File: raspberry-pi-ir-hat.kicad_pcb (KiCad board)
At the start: 2 copper layers, 56.1 x 52.3 mm, 16 parts, among them J1 IO, J2 TX, J3 RX, J4 RX_JMP, J5 TX_JMP, J6 RW_JMP, J7 Raspberry_Pi_2_3

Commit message: fix drc
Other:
- outline, holes or cut-outs redrawn
- rule pad_to_mask_clearance: 0.05 -> 0.0762
- board text added: "Add jumper for write"
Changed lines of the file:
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@@
   (general
     (thickness 1.6)
-    (drawings 10)
+    (drawings 15)
     (tracks 87)
     (zones 0)
@@
     (pad_size 1.524 1.524)
     (pad_drill 0.762)
-    (pad_to_mask_clearance 0.05)
+    (pad_to_mask_clearance 0.0762)
+    (solder_mask_min_width 0.1016)
     (aux_axis_origin 0 0)
     (visible_elements FFFFFF7F)
@@
     (descr "Through hole straight socket strip, 1x02, 2.54mm pitch, single row (from Kicad 4.0.7), script generated")
     (tags "Through hole socket strip THT 1x02 2.54mm single row")
-    (fp_text reference J6 (at 0 -2.77) (layer F.SilkS)
+    (fp_text reference J6 (at 2.54 1.27 90) (layer F.SilkS)
       (effects (font (size 1 1) (thickness 0.15)))
     )
@@
       (effects (font (size 1 1) (thickness 0.15)))
     )
+    (fp_line (start -3.2766 6.5) (end -3.2766 -6.5) (layer F.CrtYd) (width 0.12))
     (fp_line (start -3.3 -6) (end 7 -6) (layer F.SilkS) (width 0.12))
     (fp_line (start 7 -6) (end 7 6) (layer F.SilkS) (width 0.12))
@@
     (fp_line (start -3.2766 -6.5) (end 7.5 -6.5) (layer F.CrtYd) (width 0.12))
     (fp_line (start 7.5 -6.5) (end 7.5 6.5) (layer F.CrtYd) (width 0.12))
-    (fp_line (start 7.5 6.5) (end -3.2258 6.5) (layer F.CrtYd) (width 0.12))
+    (fp_line (start 7.5 6.5) (end -3.2766 6.5) (layer F.CrtYd) (width 0.12))
     (fp_line (start -3.3 -7) (end -3.3 7) (layer Cmts.User) (width 0.12))
     (pad "" thru_hole circle (at 5 0) (size 1.3 1.3) (drill 1.2) (layers *.Cu *.Mask F.SilkS))
@@
       (effects (font (size 1 1) (thickness 0.15)))
     )
+    (fp_line (start -3.2766 6.5) (end -3.2766 -6.5) (layer F.CrtYd) (width 0.12))
     (fp_line (start -3.3 -6) (end 7 -6) (layer F.SilkS) (width 0.12))
     (fp_line (start 7 -6) (end 7 6) (layer F.SilkS) (width 0.12))
@@
     (fp_line (start -3.2766 -6.5) (end 7.5 -6.5) (layer F.CrtYd) (width 0.12))
     (fp_line (start 7.5 -6.5) (end 7.5 6.5) (layer F.CrtYd) (width 0.12))
-    (fp_line (start 7.5 6.5) (end -3.2258 6.5) (layer F.CrtYd) (width 0.12))
+    (fp_line (start 7.5 6.5) (end -3.2766 6.5) (layer F.CrtYd) (width 0.12))
     (fp_line (start -3.3 -7) (end -3.3 7) (layer Cmts.User) (width 0.12))
     (pad "" thru_hole circle (at 5 0) (size 1.3 1.3) (drill 1.2) (layers *.Cu *.Mask F.SilkS))
@@
     )
   )
-  (gr_text https://github.com/joeferner/raspberry-pi-ir-hat (at 159.258 138.176) (layer F.SilkS)
+  (gr_text "Add jumper\nfor write" (at 183.896 131.572) (layer F.SilkS)
+    (effects (font (size 0.762 0.762) (thickness 0.1016)))
+  )
+  (gr_arc (start 138.684 88.646) (end 138.684 88.138) (angle -90) (layer Edge.Cuts) (width 0.05))
+  (gr_arc (start 138.684 139.954) (end 138.176 139.954) (angle -90) (layer Edge.Cuts) (width 0.05))
+  (gr_arc (start 193.802 139.954) (end 193.802 140.462) (angle -90) (layer Edge.Cuts) (width 0.05))
+  (gr_arc (start 193.802 88.646) (end 194.31 88.646) (angle -90) (layer Edge.Cuts) (width 0.05))
+  (gr_text https://github.com/joeferner/raspberry-pi-ir-hat (at 159.766 132.588) (layer F.SilkS)
     (effects (font (size 1 1) (thickness 0.15)))
   )
-  (gr_text 2020-09-11 (at 158.496 136.144) (layer F.SilkS)
+  (gr_text 2020-09-11 (at 159.004 128.524) (layer F.SilkS)
     (effects (font (size 1 1) (thickness 0.15)))
   )
-  (gr_text "Raspberry PI IR Tx/Rx" (at 158.496 134.112) (layer F.SilkS)
+  (gr_text "Raspberry PI IR Tx/Rx" (at 159.258 124.46) (layer F.SilkS)
     (effects (font (size 1 1) (thickness 0.15)))
   )
@@
     (effects (font (size 1 1) (thickness 0.15)))
   )
-  (gr_line (start 138.176 88.138) (end 194.31 88.138) (layer Edge.Cuts) (width 0.05))
-  (gr_line (start 138.176 140.462) (end 138.176 88.138) (layer Edge.Cuts) (width 0.05))
-  (gr_line (start 194.31 140.462) (end 138.176 140.462) (layer Edge.Cuts) (width 0.05))
-  (gr_line (start 194.31 88.138) (end 194.31 140.462) (layer Edge.Cuts) (width 0.05))
+  (gr_line (start 138.684 88.138) (end 193.802 88.138) (layer Edge.Cuts) (width 0.05))
+  (gr_line (start 138.176 139.954) (end 138.176 88.646) (layer Edge.Cuts) (width 0.05))
+  (gr_line (start 193.802 140.462) (end 138.684 140.462) (layer Edge.Cuts) (width 0.05))
+  (gr_line (start 194.31 88.646) (end 194.31 139.954) (layer Edge.Cuts) (width 0.05))
   (segment (start 159.923 107.539) (end 160.274 107.188) (width 0.254) (layer F.Cu) (net 1))
   (via (at 160.274 107.188) (size 0.508) (drill 0.254) (layers F.Cu B.Cu) (net 1))
@@
     (polygon
       (pts
-        (xy 193.802 139.954) (xy 138.684 139.954) (xy 138.684 88.646) (xy 193.802 88.646)
+        (xy 193.294 139.446) (xy 139.192 139.446) (xy 139.192 89.154) (xy 193.294 89.154)
       )
     )
@@
     (polygon
       (pts
-        (xy 193.802 139.954) (xy 138.684 139.954) (xy 138.684 88.646) (xy 193.802 88.646)
+        (xy 193.294 139.7) (xy 139.192 139.446) (xy 139.192 89.154) (xy 193.294 89.154)
       )
     )

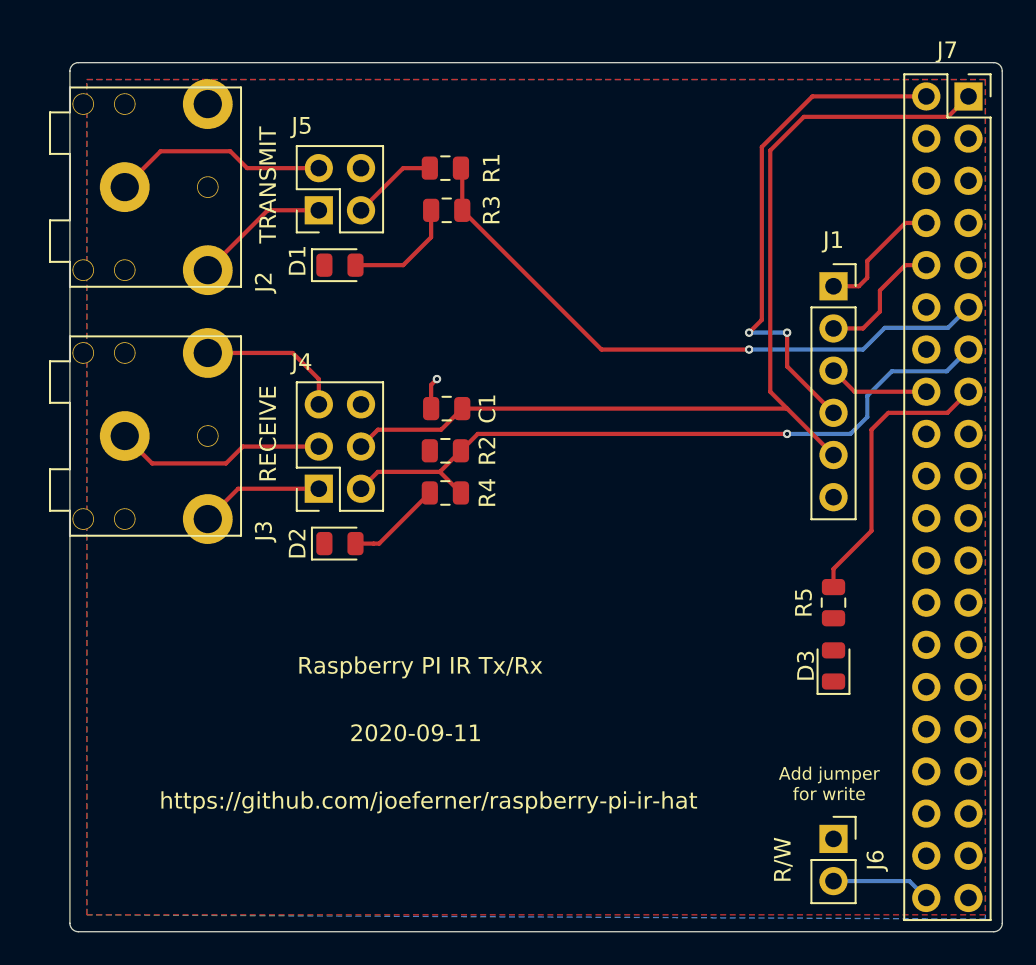
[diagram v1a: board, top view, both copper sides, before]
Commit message: add labels
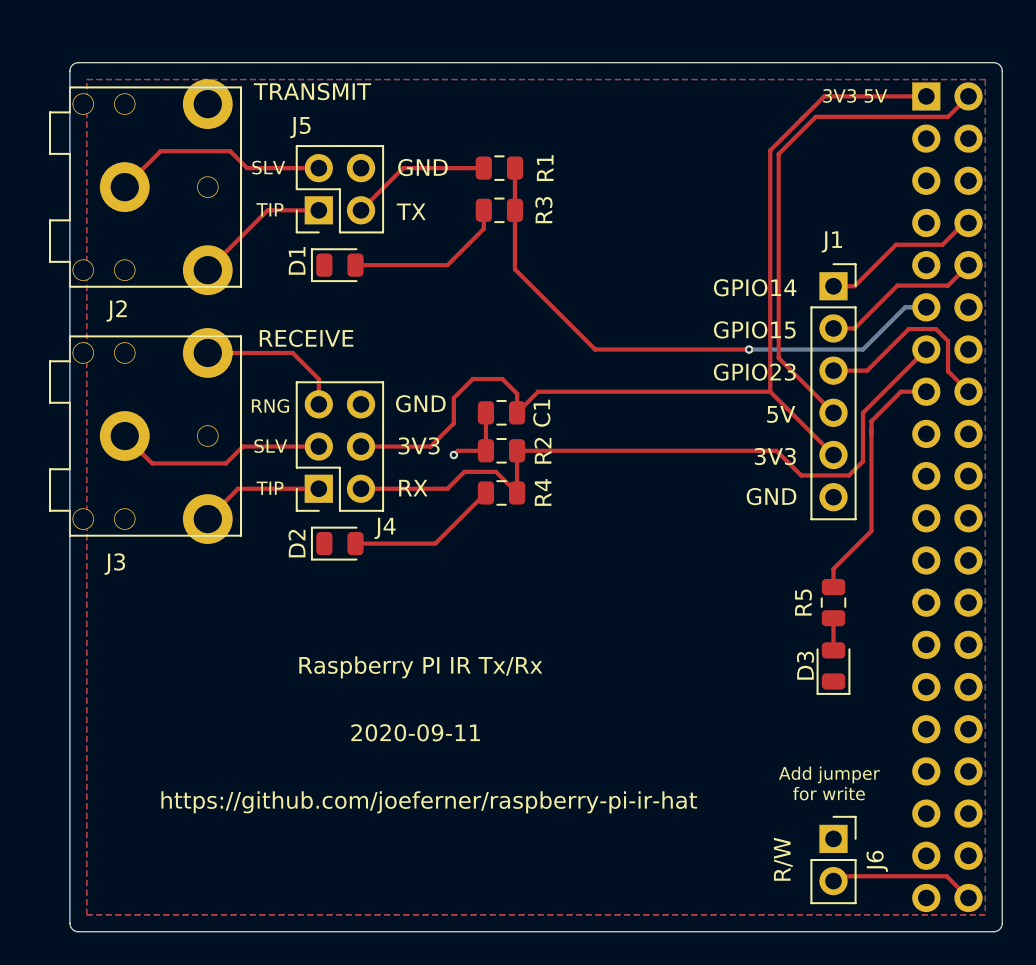
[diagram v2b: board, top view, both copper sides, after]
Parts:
- J7: moved to B.Cu
- moved R2 3.38 mm to (164.2, 111.5)
- moved R4 3.38 mm to (164.2, 114.0)
- moved C1 3.31 mm to (164.2, 109.2)
- moved R1 3.25 mm to (164.0, 94.5)
- moved R3 3.18 mm to (164.0, 97.0)
- moved J7 2.54 mm to (189.7, 90.2), turned to 180 degrees
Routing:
- net /IO3: track 6.11 -> 11.8 mm
- net /TX: track 37.6 -> 33.9 mm
- net Net-(D2-Pad2): track 5.74 -> 9.12 mm
- net Net-(J5-Pad2): track 5.19 -> 8.45 mm
- net Net-(D1-Pad2): track 6.87 -> 9.75 mm
- net /RW: track 6.01 -> 8.79 mm
- net GND: track 1.92 -> 4.33 mm
- net /MISC: track 17.2 -> 15.2 mm
- net /IO1: track 7.76 -> 9.71 mm
- net Net-(D3-Pad2): track 0.00 -> 1.93 mm
- net /IO2: track 7.91 -> 9.71 mm
- net /5V: track 30.9 -> 29.8 mm, vias 2 -> 0
- net /RX: track 42.6 -> 43.0 mm, vias 1 -> 0
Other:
- board text added: "3V3"
- board text added: "3V3 5V"
- board text added: "5V"
- board text added: "GND"
- board text added: "GPIO14"
- board text added: "GPIO15"
- board text added: "GPIO23"
- board text added: "RNG"
- board text added: "RX"
- board text added: "SLV"
- board text added: "TIP"
- board text added: "TX"

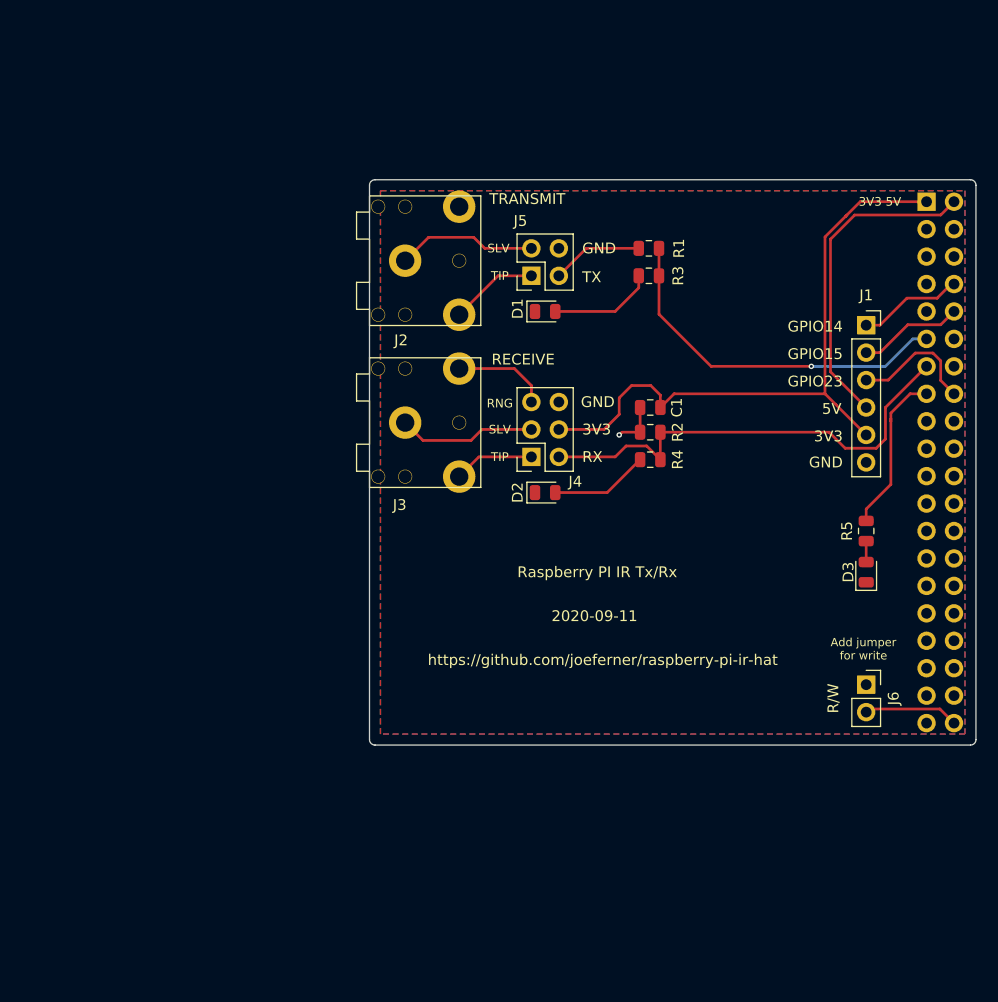
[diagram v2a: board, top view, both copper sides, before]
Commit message: Flip hat to outside
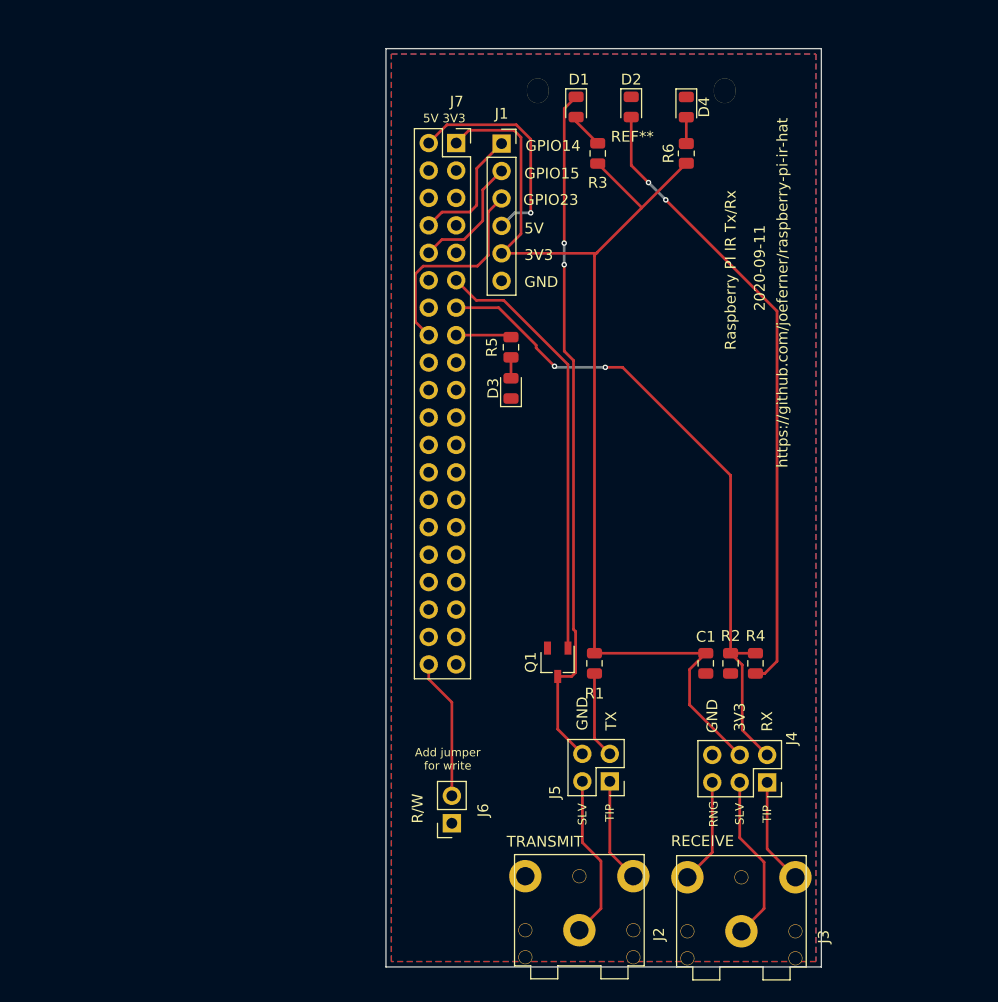
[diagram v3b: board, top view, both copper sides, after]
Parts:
- added D4: RX, LED_SMD:LED_0805_2012Metric, F.Cu at (167.5, 81.4)
- added Q1: Q_NMOS_GSD, Package_TO_SOT_SMD:TSOT-23, F.Cu at (155.6, 132.8)
- added R6: 1K, Resistor_SMD:R_0805_2012Metric, F.Cu at (167.5, 85.7)
- added REF**: BIVAR-RLP3-200-500, modules:BIVAR-RLP3-200-500, F.Cu at (162.4, 81.2)
- J7: moved to F.Cu
- moved J2 64.0 mm to (157.6, 157.6), turned to 90 degrees
- moved J3 56.4 mm to (172.6, 157.7), turned to 90 degrees
- moved J5 47.3 mm to (160.4, 143.8), turned to 270 degrees
- moved J7 43.9 mm to (146.2, 84.7), turned to 0 degrees
- moved J6 40.4 mm to (145.8, 147.7), turned to 180 degrees
- moved R1 38.7 mm to (159.0, 132.9), turned to 90 degrees
- moved J1 37.7 mm to (150.4, 84.8)
- moved J4 37.2 mm to (175.0, 143.9), turned to 270 degrees
- moved R5 37.0 mm to (151.3, 103.6)
- moved D3 37.0 mm to (151.3, 107.5)
- moved D2 36.6 mm to (162.4, 81.4), turned to 270 degrees
- moved C1 24.2 mm to (169.3, 132.9), turned to 270 degrees
- moved R2 22.6 mm to (171.6, 132.9), turned to 270 degrees
- moved R4 21.2 mm to (173.9, 132.9), turned to 270 degrees
- moved D1 19.1 mm to (157.3, 81.4), turned to 270 degrees
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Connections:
- D1 pad 1: GND -> Net-(D1-Pad1)
- J5 pad 4: GND -> Net-(D1-Pad1)
- R1 pad 1: /TX -> Net-(J5-Pad2)
- R1 pad 2: Net-(J5-Pad2) -> VCC
- R3 pad 1: /TX -> VCC
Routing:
- net Net-(D1-Pad1): track 0.00 -> 64.1 mm, vias 0 -> 2
- net Net-(D2-Pad2): track 9.12 -> 58.4 mm, vias 0 -> 2
- net VCC: track 60.1 -> 104.1 mm
- net /RX: track 43.0 -> 61.6 mm, vias 0 -> 2
- net /MISC: track 15.2 -> 5.15 mm
- net /5V: track 29.8 -> 20.7 mm, vias 0 -> 1
- net /IO3: track 11.8 -> 19.4 mm
- net Net-(D1-Pad2): track 9.75 -> 3.25 mm
- net /TX: track 33.9 -> 39.8 mm, vias 1 -> 0
- net GND: track 4.33 -> 0.00 mm, vias 1 -> 0
- net /RW: track 8.79 -> 13.0 mm
- net Net-(J3-Pad1): track 12.8 -> 15.6 mm
- net Net-(D4-Pad2): track 0.00 -> 2.44 mm
- net Net-(J3-Pad2): track 7.44 -> 9.87 mm
- net Net-(J2-Pad1): track 13.0 -> 15.3 mm
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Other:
- board size 56.1 x 52.3 mm -> 40.3 x 85 mm
- board text added: "5V 3V3"
- board text removed: "3V3 5V"

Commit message: wip
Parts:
- J1: footprint Connector_PinSocket_2.54mm:PinSocket_1x06_P2.54mm_Vertical -> Connector_PinHeader_2.54mm:PinHeader_1x06_P2.54mm_Vertical
- J4: footprint Connector_PinSocket_2.54mm:PinSocket_2x03_P2.54mm_Vertical -> Connector_PinHeader_2.54mm:PinHeader_2x03_P2.54mm_Vertical
- J5: footprint Connector_PinSocket_2.54mm:PinSocket_2x02_P2.54mm_Vertical -> Connector_PinHeader_2.54mm:PinHeader_2x02_P2.54mm_Vertical
- J6: footprint Connector_PinSocket_2.54mm:PinSocket_1x02_P2.54mm_Vertical -> Connector_PinHeader_2.54mm:PinHeader_1x02_P2.54mm_Vertical
- moved J4 5.09 mm to (169.9, 143.7), turned to 90 degrees
- moved J5 2.52 mm to (157.9, 143.7), turned to 90 degrees
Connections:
- J4 pad 1: Net-(J3-Pad2) -> Net-(J3-Pad3)
- J4 pad 2: /RX -> GND
- J4 pad 5: Net-(J3-Pad3) -> Net-(J3-Pad2)
- J4 pad 6: GND -> /RX
- J5 pad 1: Net-(J2-Pad2) -> Net-(J2-Pad1)
- J5 pad 2: Net-(J5-Pad2) -> Net-(D1-Pad1)
- J5 pad 3: Net-(J2-Pad1) -> Net-(J2-Pad2)
- J5 pad 4: Net-(D1-Pad1) -> Net-(J5-Pad4)
- R1 pad 1: Net-(J5-Pad2) -> Net-(J5-Pad4)
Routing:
- net Net-(J5-Pad4): track 0.00 -> 8.03 mm
- net Net-(J5-Pad2): track 8.03 -> 0.00 mm
- net GND: track 0.00 -> 1.77 mm, vias 0 -> 1

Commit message: wip
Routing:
- net GND: vias 1 -> 19

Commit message: 2020-10-01
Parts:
- moved D4 49.4 mm to (118.1, 81.0)
- moved R6 49.4 mm to (118.1, 85.3)
- moved J5 44.1 mm to (113.8, 143.8)
- moved J2 44.1 mm to (113.5, 157.7)
- moved J4 43.8 mm to (126.1, 143.7)
- moved J3 43.8 mm to (128.8, 157.7)
- moved C1 41.9 mm to (127.4, 131.0)
- moved R1 41.9 mm to (117.1, 131.0)
- moved R2 41.9 mm to (129.7, 131.0), turned to 90 degrees
- moved R4 41.9 mm to (132.0, 131.0), turned to 90 degrees
- moved Q1 41.9 mm to (113.7, 130.9)
- moved REF** 39.2 mm to (123.2, 80.8)
- moved R3 36.1 mm to (123.2, 85.3)
- moved D1 34.1 mm to (123.2, 80.9)
- moved D2 34.1 mm to (128.3, 80.9)
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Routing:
- net /5V: track 20.7 -> 49.8 mm, vias 1 -> 0
- net /TX: track 39.8 -> 60.1 mm, vias 0 -> 3
- net /MISC: track 5.15 -> 22.6 mm
- net VCC: track 104.1 -> 117.2 mm, vias 0 -> 2
- net /RW: track 13.0 -> 21.7 mm
- net Net-(D1-Pad1): track 64.1 -> 70.4 mm
- net /IO3: track 19.4 -> 14.1 mm
- net /RX: track 61.6 -> 66.8 mm, vias 2 -> 0
- net /IO2: track 11.6 -> 16.2 mm
- net /IO1: track 11.9 -> 16.2 mm
- net Net-(J5-Pad4): track 8.03 -> 9.66 mm
- net GND: track 1.77 -> 3.27 mm, vias 19 -> 16
- net Net-(D2-Pad2): track 58.4 -> 57.0 mm
- net Net-(D1-Pad2): track 3.25 -> 2.51 mm
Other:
- board size 40.3 x 85 mm -> 42.7 x 85 mm
- rule solder_mask_min_width: 0.1016 -> 0.127
- board text added: "2020-10-01"
- board text added: "MISC"
- board text added: "PWR"
- board text removed: "2020-09-11"
